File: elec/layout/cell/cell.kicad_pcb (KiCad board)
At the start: 4 copper layers, 79.5 x 8 mm, 65 parts

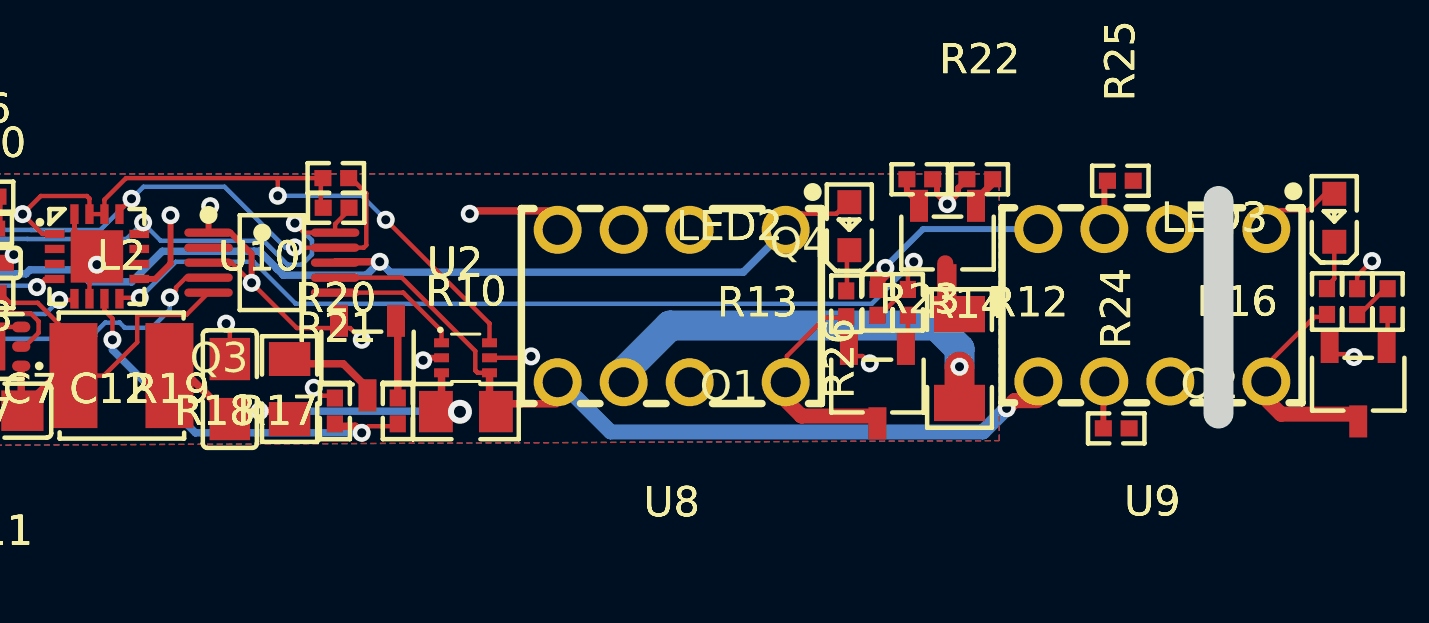
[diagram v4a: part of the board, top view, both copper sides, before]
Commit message: Update cell layouts
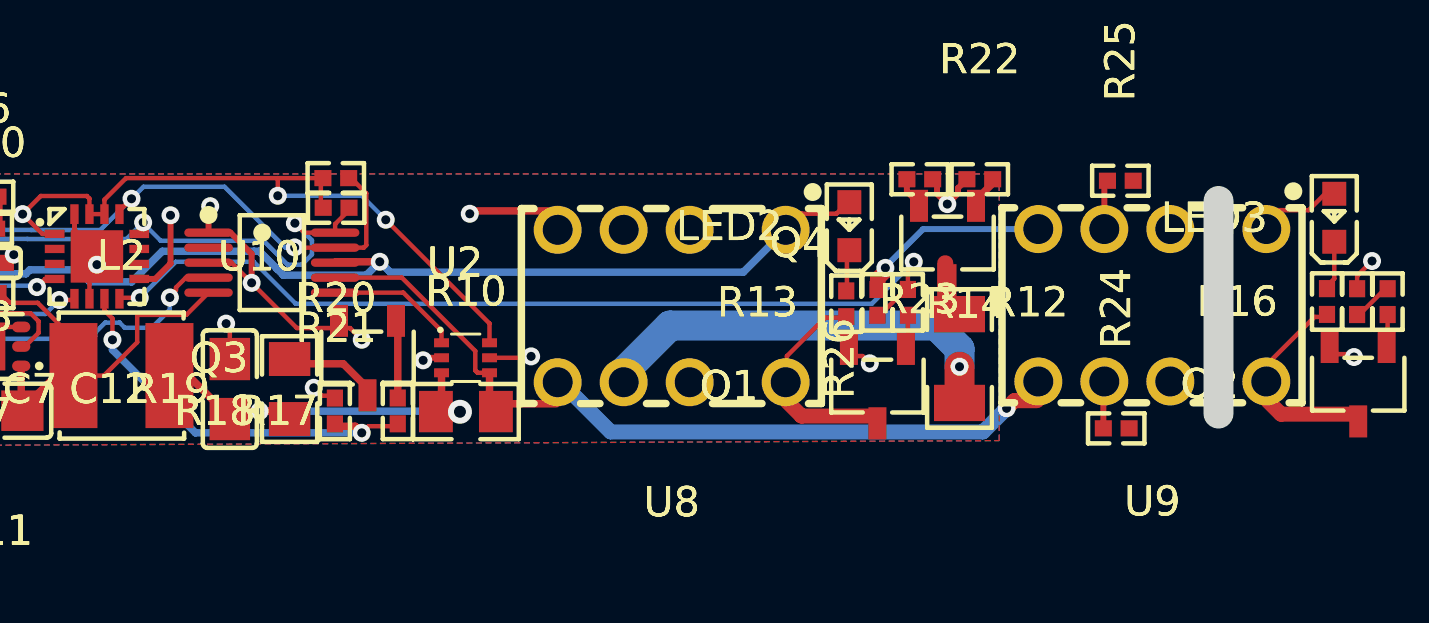
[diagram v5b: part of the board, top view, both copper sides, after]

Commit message: tidy up isolated supplies
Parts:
- R6: value 43kΩ ±1% 62.5mW -> 43.2kΩ ±1% 62.5mW
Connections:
- C1 pad 1: hv -> hv-5
- C1 pad 2: gnd-8 -> gnd-1
- C10 pad 1: hv-9 -> hv-8
- C10 pad 2: gnd -> gnd-7
- C11 pad 1: hv-9 -> hv-8
- C11 pad 2: gnd -> gnd-7
- C12 pad 1: hv-5 -> hv-6
- C12 pad 2: gnd -> gnd-7
- C13 pad 2: gnd-5 -> gnd-9
- C14 pad 2: gnd-5 -> gnd-9
- C15 pad 2: gnd -> gnd-7
- C16 pad 2: gnd -> gnd-7
- C2 pad 2: gnd -> gnd-7
- C3 pad 2: gnd -> gnd-7
- C4 pad 2: gnd -> gnd-7
- C5 pad 2: gnd -> gnd-7
- C6 pad 1: hv-7 -> hv
- C6 pad 2: gnd -> gnd-7
- C7 pad 1: hv-7 -> hv
- C7 pad 2: gnd -> gnd-7
- C8 pad 1: hv-7 -> hv
- C8 pad 2: gnd -> gnd-7
- L1 pad 2: hv-7 -> hv
- L2 pad 1: hv-9 -> hv-8
- L2 pad 2: hv-5 -> hv-6
- LED3 pad 2: hv-2 -> hv-7
- Q1 pad 2: gnd -> gnd-7
- Q3 pad 2: gnd -> gnd-7
- Q3 pad 3: gnd-2 -> gnd
- Q4 pad 2: gnd-7 -> gnd-2
- Q4 pad 3: gnd-1 -> gnd-6
- R10 pad 1: hv-5 -> hv-6
- R10 pad 2: hv-8 -> hv-10
- R11 pad 2: gnd -> gnd-7
- R12 pad 1: line-4 -> line-10
- R13 pad 1: line-4 -> line-10
- R13 pad 2: gnd -> gnd-7
- R15 pad 1: line-7 -> line-5
- R16 pad 1: line-7 -> line-5
- R17 pad 1: line-11 -> line-3
- R18 pad 1: line-11 -> line-3
- R18 pad 2: gnd -> gnd-7
- R19 pad 1: hv-5 -> hv-6
- R19 pad 2: gnd-2 -> gnd
- R20 pad 1: line-6 -> line-4
- R21 pad 1: line-10 -> line-6
- R22 pad 1: line-1 -> line-9
- R23 pad 1: line-1 -> line-9
- R23 pad 2: gnd-7 -> gnd-2
- R24 pad 1: hv-6 -> hv-1
- R24 pad 2: hv-4 -> hv-3
- R25 pad 1: gnd-6 -> gnd-4
- R26 pad 1: hv-3 -> hv-4
- R26 pad 2: gnd-1 -> gnd-6
- R3 pad 1: hv-7 -> hv
- R4 pad 2: gnd -> gnd-7
- R5 pad 1: line-5 -> line
- R7 pad 1: hv-9 -> hv-8
- R8 pad 2: gnd -> gnd-7
- R9 pad 1: line-2 -> line-7
- U1 pad 1: hv -> hv-5
- U1 pad 2: gnd-8 -> gnd-1
- U1 pad 4: gnd -> gnd-7
- U10 pad 10: gpio-net-2 -> gpio-net
- U10 pad 12: line-10 -> line-6
- U10 pad 13: line-6 -> line-4
- U10 pad 16: gnd -> gnd-7
- U10 pad 17: gnd -> gnd-7
- U10 pad 2: gpio-net -> gpio-net-1
- U10 pad 3: gpio-net-1 -> gpio-net-2
- U10 pad 4: line-5 -> line
- U10 pad 5: line-2 -> line-7
- U10 pad 6: gnd -> gnd-7
- U10 pad 7: line-11 -> line-3
- U10 pad 8: line-4 -> line-10
- U10 pad 9: line-1 -> line-9
- U11 pad 1: hv-1 -> hv-9
- U11 pad 2: line-3 -> line-2
- U11 pad 3: line-8 -> line-1
- U11 pad 4: gnd-4 -> gnd-8
- U11 pad 5: gnd -> gnd-7
- U11 pad 6: line-10 -> line-6
- U11 pad 7: line-6 -> line-4
- U12 pad 3: gnd-5 -> gnd-9
- U12 pad 4: line-9 -> line-11
- U13 pad 2: line-9 -> line-11
- U13 pad 3: gnd-5 -> gnd-9
- U14 pad 1: gnd -> gnd-7
- U2 pad 1: gnd -> gnd-7
- U2 pad 10: line-10 -> line-6
- U2 pad 3: gnd -> gnd-7
- U2 pad 4: hv-7 -> hv
- U2 pad 5: hv-9 -> hv-8
- U2 pad 6: line -> line-8
- U2 pad 7: hv-8 -> hv-10
- U2 pad 9: line-6 -> line-4
- U3 pad 2: gnd -> gnd-7
- U3 pad 4: line-6 -> line-4
- U3 pad 5: line-10 -> line-6
- U4 pad 1: gnd -> gnd-7
- U5 pad 2: gnd -> gnd-7
- U5 pad 4: line-6 -> line-4
- U5 pad 5: line-10 -> line-6
- U5 pad 6: gnd -> gnd-7
- U6 pad 1: hv-9 -> hv-8
- U6 pad 3: gnd -> gnd-7
- U6 pad 6: hv-7 -> hv
- U6 pad 7: gnd -> gnd-7
- U7 pad 1: line -> line-8
- U7 pad 2: gnd -> gnd-7
- U7 pad 3: hv-5 -> hv-6
- U7 pad 4: hv-8 -> hv-10
- U7 pad 5: gnd -> gnd-7
- U8 pad 3: gnd-7 -> gnd-2
- U8 pad 4: gnd -> gnd-7
- U8 pad 5: hv-8 -> hv-10
- U8 pad 6: hv-3 -> hv-4
- U9 pad 1: hv-2 -> hv-7
- U9 pad 3: gnd-6 -> gnd-4
- U9 pad 4: gnd -> gnd-7
- U9 pad 5: hv-8 -> hv-10
- U9 pad 6: hv-6 -> hv-1
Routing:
- net gnd-7: track 1.30 -> 105.5 mm, vias 0 -> 31
- net gnd: track 105.5 -> 3.42 mm, vias 31 -> 0
- net line-1: track 31.7 -> 0.00 mm, vias 2 -> 0
- net line-9: track 2.29 -> 31.7 mm, vias 0 -> 2
- net hv-10: track 0.00 -> 27.5 mm, vias 0 -> 1
- net hv-7: track 24.3 -> 2.26 mm, vias 2 -> 0
- net hv: track 4.33 -> 24.3 mm, vias 0 -> 2
- net hv-9: track 15.6 -> 0.00 mm
- net hv-4: track 0.00 -> 14.3 mm, vias 0 -> 1
- net hv-3: track 14.3 -> 0.00 mm, vias 1 -> 0
- net line-4: track 30.4 -> 44.5 mm, vias 2 -> 4
- net line-3: track 0.00 -> 13.5 mm, vias 0 -> 2
- net line-10: track 43.5 -> 30.4 mm, vias 5 -> 2
- net hv-8: track 27.5 -> 15.6 mm, vias 1 -> 0
- net hv-6: track 1.58 -> 13.2 mm, vias 0 -> 2
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- added copper zone on B.Cu, net gnd-7
- added copper zone on F.Cu, net gnd-7
- added copper zone on In2.Cu, net gnd-7
- removed copper zone on B.Cu, net gnd
- removed copper zone on F.Cu, net gnd
- removed copper zone on In2.Cu, net gnd

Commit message: building frozen
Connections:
- C1 pad 1: hv-5 -> hv-3
- C1 pad 2: gnd-1 -> gnd-6
- C10 pad 1: hv-8 -> hv-6
- C11 pad 1: hv-8 -> hv-6
- C12 pad 1: hv-6 -> hv-8
- C13 pad 1: hv-2 -> hv-5
- C13 pad 2: gnd-9 -> gnd-2
- C14 pad 1: hv-2 -> hv-5
- C14 pad 2: gnd-9 -> gnd-2
- L2 pad 1: hv-8 -> hv-6
- L2 pad 2: hv-6 -> hv-8
- LED3 pad 2: hv-7 -> hv-5
- Q2 pad 2: gnd-5 -> gnd-2
- Q3 pad 3: gnd -> gnd-3
- Q4 pad 2: gnd-2 -> gnd-8
- Q4 pad 3: gnd-6 -> gnd-4
- R10 pad 1: hv-6 -> hv-8
- R10 pad 2: hv-10 -> hv-4
- R12 pad 1: line-10 -> line-8
- R13 pad 1: line-10 -> line-8
- R15 pad 1: line-5 -> line-11
- R16 pad 1: line-5 -> line-11
- R16 pad 2: gnd-5 -> gnd-2
- R17 pad 1: line-3 -> line-2
- R18 pad 1: line-3 -> line-2
- R19 pad 1: hv-6 -> hv-8
- R19 pad 2: gnd -> gnd-3
- R20 pad 1: line-4 -> line-1
- R21 pad 1: line-6 -> line-9
- R22 pad 1: line-9 -> line-10
- R23 pad 1: line-9 -> line-10
- R23 pad 2: gnd-2 -> gnd-8
- R24 pad 1: hv-1 -> hv-7
- R24 pad 2: hv-3 -> hv-2
- R25 pad 1: gnd-4 -> gnd
- R25 pad 2: gnd-3 -> gnd-5
- R26 pad 1: hv-4 -> hv-9
- R26 pad 2: gnd-6 -> gnd-4
- R5 pad 1: line -> line-5
- R7 pad 1: hv-8 -> hv-6
- R9 pad 1: line-7 -> line-3
- U1 pad 1: hv-5 -> hv-3
- U1 pad 2: gnd-1 -> gnd-6
- U10 pad 10: gpio-net -> gpio-net-2
- U10 pad 12: line-6 -> line-9
- U10 pad 13: line-4 -> line-1
- U10 pad 2: gpio-net-1 -> gpio-net
- U10 pad 3: gpio-net-2 -> gpio-net-1
- U10 pad 4: line -> line-5
- U10 pad 5: line-7 -> line-3
- U10 pad 7: line-3 -> line-2
- U10 pad 8: line-10 -> line-8
- U10 pad 9: line-9 -> line-10
- U11 pad 1: hv-9 -> hv-1
- U11 pad 2: line-2 -> line-7
- U11 pad 3: line-1 -> line-4
- U11 pad 4: gnd-8 -> gnd-1
- U11 pad 6: line-6 -> line-9
- U11 pad 7: line-4 -> line-1
- U12 pad 1: hv-2 -> hv-5
- U12 pad 3: gnd-9 -> gnd-2
- U12 pad 4: line-11 -> line-6
- U13 pad 1: hv-2 -> hv-5
- U13 pad 2: line-11 -> line-6
- U13 pad 3: gnd-9 -> gnd-2
- U2 pad 10: line-6 -> line-9
- U2 pad 5: hv-8 -> hv-6
- U2 pad 6: line-8 -> line
- U2 pad 7: hv-10 -> hv-4
- U2 pad 9: line-4 -> line-1
- U3 pad 4: line-4 -> line-1
- U3 pad 5: line-6 -> line-9
- U5 pad 4: line-4 -> line-1
- U5 pad 5: line-6 -> line-9
- U6 pad 1: hv-8 -> hv-6
- U7 pad 1: line-8 -> line
- U7 pad 3: hv-6 -> hv-8
- U7 pad 4: hv-10 -> hv-4
- U8 pad 3: gnd-2 -> gnd-8
- U8 pad 5: hv-10 -> hv-4
- U8 pad 6: hv-4 -> hv-9
- U9 pad 1: hv-7 -> hv-5
- U9 pad 3: gnd-4 -> gnd
- U9 pad 5: hv-10 -> hv-4
- U9 pad 6: hv-1 -> hv-7
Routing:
- net line-4: track 44.5 -> 0.00 mm, vias 4 -> 0
- net line-1: track 0.00 -> 44.5 mm, vias 0 -> 4
- net line-6: track 43.5 -> 2.29 mm, vias 5 -> 0
- net hv-10: track 27.5 -> 0.00 mm, vias 1 -> 0
- net line-8: track 4.47 -> 30.4 mm, vias 0 -> 2
- net (no net): track 0.00 -> 15.3 mm, vias 0 -> 7
- net hv-9: track 0.00 -> 14.3 mm, vias 0 -> 1
- net line-2: track 0.00 -> 13.5 mm, vias 0 -> 2
- net hv-4: track 14.3 -> 27.5 mm
- net line-9: track 31.7 -> 43.5 mm, vias 2 -> 5
- net line-5: track 1.44 -> 12.8 mm, vias 0 -> 2
- net gnd-1: track 10.8 -> 0.00 mm, vias 1 -> 0
- net gnd-6: track 1.89 -> 10.8 mm, vias 0 -> 1
- net line: track 12.8 -> 4.47 mm, vias 2 -> 0
- net hv-2: track 7.79 -> 0.00 mm, vias 1 -> 0
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
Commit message: Build everything with ordered params to fix frozen builds
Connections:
- C1 pad 2: gnd-6 -> gnd-3
- C10 pad 1: hv-6 -> hv-5
- C10 pad 2: gnd-7 -> gnd-8
- C11 pad 1: hv-6 -> hv-5
- C11 pad 2: gnd-7 -> gnd-8
- C12 pad 1: hv-8 -> hv
- C12 pad 2: gnd-7 -> gnd-8
- C13 pad 1: hv-5 -> hv-2
- C13 pad 2: gnd-2 -> gnd
- C14 pad 1: hv-5 -> hv-2
- C14 pad 2: gnd-2 -> gnd
- C15 pad 2: gnd-7 -> gnd-8
- C16 pad 2: gnd-7 -> gnd-8
- C2 pad 2: gnd-7 -> gnd-8
- C3 pad 2: gnd-7 -> gnd-8
- C4 pad 2: gnd-7 -> gnd-8
- C5 pad 2: gnd-7 -> gnd-8
- C6 pad 1: hv -> hv-6
- C6 pad 2: gnd-7 -> gnd-8
- C7 pad 1: hv -> hv-6
- C7 pad 2: gnd-7 -> gnd-8
- C8 pad 1: hv -> hv-6
- C8 pad 2: gnd-7 -> gnd-8
- L1 pad 2: hv -> hv-6
- L2 pad 1: hv-6 -> hv-5
- L2 pad 2: hv-8 -> hv
- LED3 pad 2: hv-5 -> hv-2
- Q1 pad 2: gnd-7 -> gnd-8
- Q2 pad 2: gnd-2 -> gnd
- Q3 pad 2: gnd-7 -> gnd-8
- Q3 pad 3: gnd-3 -> gnd-5
- Q4 pad 2: gnd-8 -> gnd-2
- R10 pad 1: hv-8 -> hv
- R10 pad 2: hv-4 -> hv-8
- R11 pad 2: gnd-7 -> gnd-8
- R12 pad 1: line-8 -> line-2
- R13 pad 1: line-8 -> line-2
- R13 pad 2: gnd-7 -> gnd-8
- R15 pad 1: line-11 -> line-4
- R16 pad 1: line-11 -> line-4
- R16 pad 2: gnd-2 -> gnd
- R17 pad 1: line-2 -> line-1
- R18 pad 1: line-2 -> line-1
- R18 pad 2: gnd-7 -> gnd-8
- R19 pad 1: hv-8 -> hv
- R19 pad 2: gnd-3 -> gnd-5
- R20 pad 1: line-1 -> line-7
- R21 pad 1: line-9 -> line-8
- R22 pad 1: line-10 -> line-11
- R23 pad 1: line-10 -> line-11
- R23 pad 2: gnd-8 -> gnd-2
- R24 pad 1: hv-7 -> hv-4
- R24 pad 2: hv-2 -> hv-9
- R25 pad 1: gnd -> gnd-7
- R25 pad 2: gnd-5 -> gnd-1
- R26 pad 1: hv-9 -> hv-7
- R3 pad 1: hv -> hv-6
- R4 pad 2: gnd-7 -> gnd-8
- R5 pad 1: line-5 -> line-6
- R7 pad 1: hv-6 -> hv-5
- R8 pad 2: gnd-7 -> gnd-8
- U1 pad 2: gnd-6 -> gnd-3
- U1 pad 4: gnd-7 -> gnd-8
- U10 pad 10: gpio-net-2 -> gpio-net
- U10 pad 12: line-9 -> line-8
- U10 pad 13: line-1 -> line-7
- U10 pad 16: gnd-7 -> gnd-8
- U10 pad 17: gnd-7 -> gnd-8
- U10 pad 2: gpio-net -> gpio-net-1
- U10 pad 3: gpio-net-1 -> gpio-net-2
- U10 pad 4: line-5 -> line-6
- U10 pad 6: gnd-7 -> gnd-8
- U10 pad 7: line-2 -> line-1
- U10 pad 8: line-8 -> line-2
- U10 pad 9: line-10 -> line-11
- U11 pad 2: line-7 -> line
- U11 pad 3: line-4 -> line-5
- U11 pad 4: gnd-1 -> gnd-6
- U11 pad 5: gnd-7 -> gnd-8
- U11 pad 6: line-9 -> line-8
- U11 pad 7: line-1 -> line-7
- U12 pad 1: hv-5 -> hv-2
- U12 pad 3: gnd-2 -> gnd
- U12 pad 4: line-6 -> line-10
- U13 pad 1: hv-5 -> hv-2
- U13 pad 2: line-6 -> line-10
- U13 pad 3: gnd-2 -> gnd
- U14 pad 1: gnd-7 -> gnd-8
- U2 pad 1: gnd-7 -> gnd-8
- U2 pad 10: line-9 -> line-8
- U2 pad 3: gnd-7 -> gnd-8
- U2 pad 4: hv -> hv-6
- U2 pad 5: hv-6 -> hv-5
- U2 pad 6: line -> line-9
- U2 pad 7: hv-4 -> hv-8
- U2 pad 9: line-1 -> line-7
- U3 pad 2: gnd-7 -> gnd-8
- U3 pad 4: line-1 -> line-7
- U3 pad 5: line-9 -> line-8
- U4 pad 1: gnd-7 -> gnd-8
- U5 pad 2: gnd-7 -> gnd-8
- U5 pad 4: line-1 -> line-7
- U5 pad 5: line-9 -> line-8
- U5 pad 6: gnd-7 -> gnd-8
- U6 pad 1: hv-6 -> hv-5
- U6 pad 3: gnd-7 -> gnd-8
- U6 pad 6: hv -> hv-6
- U6 pad 7: gnd-7 -> gnd-8
- U7 pad 1: line -> line-9
- U7 pad 2: gnd-7 -> gnd-8
- U7 pad 3: hv-8 -> hv
- U7 pad 4: hv-4 -> hv-8
- U7 pad 5: gnd-7 -> gnd-8
- U8 pad 3: gnd-8 -> gnd-2
- U8 pad 4: gnd-7 -> gnd-8
- U8 pad 5: hv-4 -> hv-8
- U8 pad 6: hv-9 -> hv-7
- U9 pad 1: hv-5 -> hv-2
- U9 pad 3: gnd -> gnd-7
- U9 pad 4: gnd-7 -> gnd-8
- U9 pad 5: hv-4 -> hv-8
- U9 pad 6: hv-7 -> hv-4
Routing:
- net gnd-8: track 1.30 -> 105.5 mm, vias 0 -> 31
- net gnd-7: track 105.5 -> 1.66 mm, vias 31 -> 0
- net line-7: track 0.00 -> 44.5 mm, vias 0 -> 4
- net line-9: track 43.5 -> 4.47 mm, vias 5 -> 0
- net line-1: track 44.5 -> 13.5 mm, vias 4 -> 2
- net line-11: track 1.44 -> 31.7 mm, vias 0 -> 2
- net line-10: track 31.7 -> 2.29 mm, vias 2 -> 0
- net hv-4: track 27.5 -> 1.58 mm, vias 1 -> 0
- net line-2: track 13.5 -> 30.4 mm
- net hv-5: track 0.00 -> 15.6 mm
- net hv-8: track 13.2 -> 27.5 mm, vias 2 -> 1
- net hv-9: track 14.3 -> 0.00 mm, vias 1 -> 0
- net line-8: track 30.4 -> 43.5 mm, vias 2 -> 5
- net line-5: track 12.8 -> 0.00 mm, vias 2 -> 0
- net hv-7: track 1.58 -> 14.3 mm, vias 0 -> 1
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- added copper zone on B.Cu, net gnd-8
- added copper zone on F.Cu, net gnd-8
- added copper zone on In2.Cu, net gnd-8
- removed copper zone on B.Cu, net gnd-7
- removed copper zone on F.Cu, net gnd-7
- removed copper zone on In2.Cu, net gnd-7
